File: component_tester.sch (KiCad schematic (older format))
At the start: 87 parts, among them IC1 ATMEGA16U2, IC2 ATMEGA328P-A, P1 USB_OTG, P10 ICSP_prog_16u2_4, P11 BO_PC6, P12 ICSP_prog_16u2_5, P13 BO_PC5, P14 BO_PD2, P15 BO_PD3, P16 BO_PD4, P17 BO_PD5, P18 BO_PD6, P19 ICSP_prog_328_1, P2 BATTERY_CONNECTOR, P20 ICSP_prog_328_3, P21 ICSP_prog_328_4, P22 ICSP_prog_328_5, P23 CONN_01X01, P24 Device Under Test, P25 CONN_01X03, P3 Voltage_for_zener, P4 BO_PC7, P5 ICSP_prog_16u2_1, P6 BO_PD0, P7 BO_PD1, P8 BO_PC4, P9 ICSP_prog_16u2_3, Q1 TRANSISTOR_NPN_2N2222_KSP222A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, SW1 ON-OFF switch, SW2 DO_MEASUREMENT, SW3 CONNECT_CAP, U1 NCP1117ST50T3G, U2 XF2L-2625-1A, U3 LT1004, U4 CDSOT23-SRV05-4, Y1 8MHz, Y2 16MHz

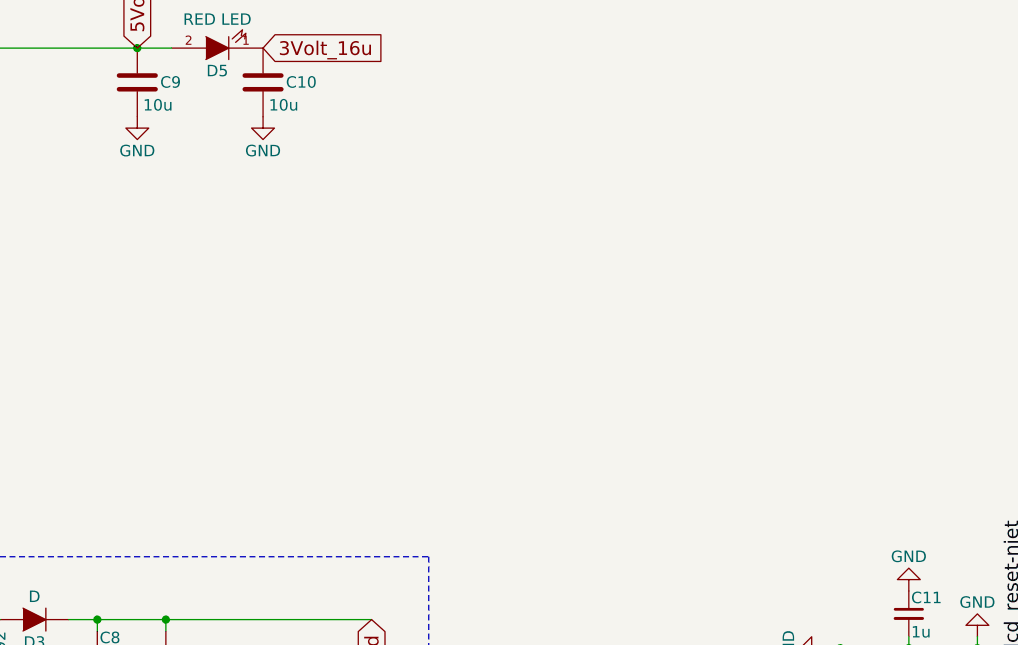
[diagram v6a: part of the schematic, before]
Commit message: Added voltage regulator option
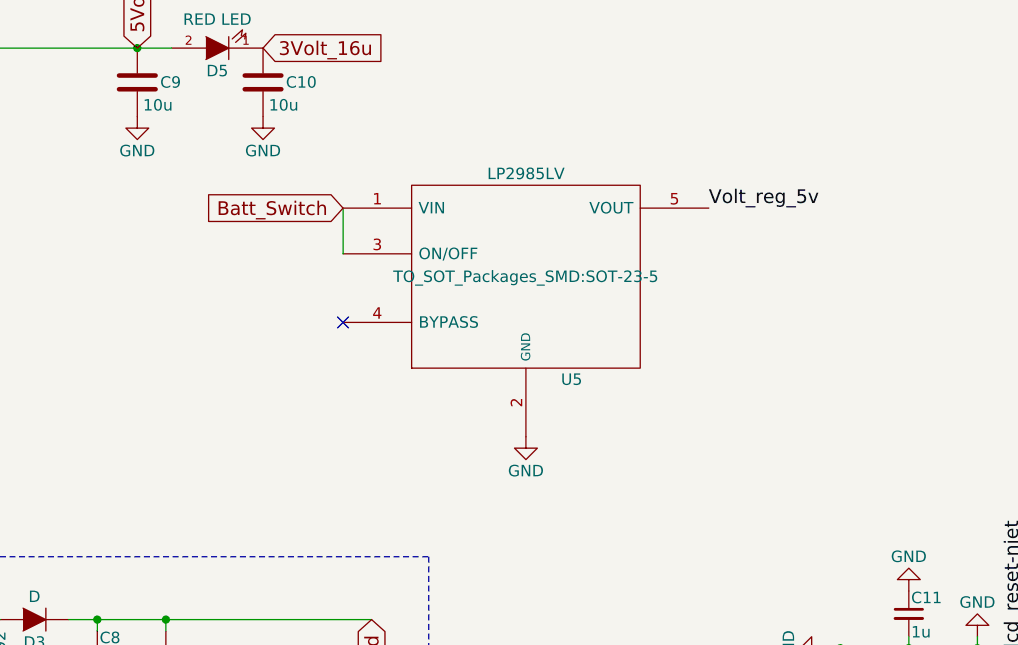
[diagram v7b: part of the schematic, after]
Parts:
- added U5: LP2985LV, TO_SOT_Packages_SMD:SOT-23-5, symbol LP2985LV
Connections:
- net Batt_Switch: now also U5.1 (VIN), U5.3 (ON/OFF)
- net GND: now also U5.2 (GND)
- net Volt_reg_5v: now also U5.5 (VOUT)
- no-connect marks 11 -> 12
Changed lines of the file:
@@
 $EndComp
 $Comp
-L GND #PWR01
+L GND #PWR27
 U 1 1 575F0F51
 P 8050 4450
-F 0 "#PWR01" H 8050 4200 50  0001 C CNN
+F 0 "#PWR27" H 8050 4200 50  0001 C CNN
 F 1 "GND" H 8050 4300 50  0000 C CNN
 F 2 "" H 8050 4450 50  0000 C CNN
@@
 $EndComp
 $Comp
-L GND #PWR02
+L GND #PWR30
 U 1 1 575F0FE6
 P 8550 6200
-F 0 "#PWR02" H 8550 5950 50  0001 C CNN
+F 0 "#PWR30" H 8550 5950 50  0001 C CNN
 F 1 "GND" H 8550 6050 50  0000 C CNN
 F 2 "" H 8550 6200 50  0000 C CNN
@@
 $EndComp
 $Comp
-L GND #PWR03
+L GND #PWR33
 U 1 1 575F1827
 P 11125 4525
-F 0 "#PWR03" H 11125 4275 50  0001 C CNN
+F 0 "#PWR33" H 11125 4275 50  0001 C CNN
 F 1 "GND" H 11125 4375 50  0000 C CNN
 F 2 "" H 11125 4525 50  0000 C CNN
@@
 3Volt_16u
 $Comp
-L GND #PWR04
+L GND #PWR18
 U 1 1 575F30CE
 P 4000 4900
-F 0 "#PWR04" H 4000 4650 50  0001 C CNN
+F 0 "#PWR18" H 4000 4650 50  0001 C CNN
 F 1 "GND" H 4000 4750 50  0000 C CNN
 F 2 "" H 4000 4900 50  0000 C CNN
@@
 $EndComp
 $Comp
-L GND #PWR05
+L GND #PWR7
 U 1 1 575F3C8E
 P 2175 3200
-F 0 "#PWR05" H 2175 2950 50  0001 C CNN
+F 0 "#PWR7" H 2175 2950 50  0001 C CNN
 F 1 "GND" H 2175 3050 50  0000 C CNN
 F 2 "" H 2175 3200 50  0000 C CNN
@@
 $EndComp
 $Comp
-L GND #PWR06
+L GND #PWR13
 U 1 1 575F41D4
 P 2900 4100
-F 0 "#PWR06" H 2900 3850 50  0001 C CNN
+F 0 "#PWR13" H 2900 3850 50  0001 C CNN
 F 1 "GND" H 2900 3950 50  0000 C CNN
 F 2 "" H 2900 4100 50  0000 C CNN
@@
 $EndComp
 $Comp
-L GND #PWR07
+L GND #PWR1
 U 1 1 575F4FF7
 P 725 3500
-F 0 "#PWR07" H 725 3250 50  0001 C CNN
+F 0 "#PWR1" H 725 3250 50  0001 C CNN
 F 1 "GND" H 725 3350 50  0000 C CNN
 F 2 "" H 725 3500 50  0000 C CNN
@@
 $EndComp
 $Comp
-L GND #PWR08
+L GND #PWR5
 U 1 1 575F552B
 P 1850 4350
-F 0 "#PWR08" H 1850 4100 50  0001 C CNN
+F 0 "#PWR5" H 1850 4100 50  0001 C CNN
 F 1 "GND" H 1850 4200 50  0000 C CNN
 F 2 "" H 1850 4350 50  0000 C CNN
@@
 $EndComp
 $Comp
-L GND #PWR09
+L GND #PWR4
 U 1 1 575F556D
 P 1625 4350
-F 0 "#PWR09" H 1625 4100 50  0001 C CNN
+F 0 "#PWR4" H 1625 4100 50  0001 C CNN
 F 1 "GND" H 1625 4200 50  0000 C CNN
 F 2 "" H 1625 4350 50  0000 C CNN
@@
 USB_Vcc
 $Comp
-L GND #PWR010
+L GND #PWR2
 U 1 1 575F563D
 P 1125 3700
-F 0 "#PWR010" H 1125 3450 50  0001 C CNN
+F 0 "#PWR2" H 1125 3450 50  0001 C CNN
 F 1 "GND" H 1125 3550 50  0000 C CNN
 F 2 "" H 1125 3700 50  0000 C CNN
@@
 $EndComp
 $Comp
-L GND #PWR011
+L GND #PWR15
 U 1 1 575F65D9
 P 3550 5750
-F 0 "#PWR011" H 3550 5500 50  0001 C CNN
+F 0 "#PWR15" H 3550 5500 50  0001 C CNN
 F 1 "GND" H 3550 5600 50  0000 C CNN
 F 2 "" H 3550 5750 50  0000 C CNN
@@
 5Volt_328
 $Comp
-L GND #PWR012
+L GND #PWR36
 U 1 1 575FC633
 P 12800 2225
-F 0 "#PWR012" H 12800 1975 50  0001 C CNN
+F 0 "#PWR36" H 12800 1975 50  0001 C CNN
 F 1 "GND" H 12800 2075 50  0000 C CNN
 F 2 "" H 12800 2225 50  0000 C CNN
@@
 $EndComp
 $Comp
-L GND #PWR013
+L GND #PWR8
 U 1 1 575FFAE7
 P 2350 3700
-F 0 "#PWR013" H 2350 3450 50  0001 C CNN
+F 0 "#PWR8" H 2350 3450 50  0001 C CNN
 F 1 "GND" H 2350 3550 50  0000 C CNN
 F 2 "" H 2350 3700 50  0000 C CNN
@@
 Battery_input
 $Comp
-L GND #PWR014
+L GND #PWR3
 U 1 1 576121F6
 P 1200 7000
-F 0 "#PWR014" H 1200 6750 50  0001 C CNN
+F 0 "#PWR3" H 1200 6750 50  0001 C CNN
 F 1 "GND" H 1200 6850 50  0000 C CNN
 F 2 "" H 1200 7000 50  0000 C CNN
@@
 $EndComp
 $Comp
-L GND #PWR015
+L GND #PWR21
 U 1 1 57613538
 P 4575 6575
-F 0 "#PWR015" H 4575 6325 50  0001 C CNN
+F 0 "#PWR21" H 4575 6325 50  0001 C CNN
 F 1 "GND" H 4575 6425 50  0000 C CNN
 F 2 "" H 4575 6575 50  0000 C CNN
@@
 $EndComp
 $Comp
-L GND #PWR016
+L GND #PWR22
 U 1 1 5761377B
 P 5125 6575
-F 0 "#PWR016" H 5125 6325 50  0001 C CNN
+F 0 "#PWR22" H 5125 6325 50  0001 C CNN
 F 1 "GND" H 5125 6425 50  0000 C CNN
 F 2 "" H 5125 6575 50  0000 C CNN
@@
 $EndComp
 $Comp
-L GND #PWR017
+L GND #PWR25
 U 1 1 5761F9F4
 P 7850 3125
-F 0 "#PWR017" H 7850 2875 50  0001 C CNN
+F 0 "#PWR25" H 7850 2875 50  0001 C CNN
 F 1 "GND" H 7850 2975 50  0000 C CNN
 F 2 "" H 7850 3125 50  0000 C CNN
@@
 $EndComp
 $Comp
-L GND #PWR018
+L GND #PWR35
 U 1 1 57622493
 P 11850 5925
-F 0 "#PWR018" H 11850 5675 50  0001 C CNN
+F 0 "#PWR35" H 11850 5675 50  0001 C CNN
 F 1 "GND" H 11850 5775 50  0000 C CNN
 F 2 "" H 11850 5925 50  0000 C CNN
@@
 $EndComp
 $Comp
-L GND #PWR019
+L GND #PWR16
 U 1 1 576263B2
 P 3650 2000
-F 0 "#PWR019" H 3650 1750 50  0001 C CNN
+F 0 "#PWR16" H 3650 1750 50  0001 C CNN
 F 1 "GND" H 3650 1850 50  0000 C CNN
 F 2 "" H 3650 2000 50  0000 C CNN
@@
 3Volt_16u
 $Comp
-L GND #PWR020
+L GND #PWR31
 U 1 1 57602456
 P 9550 8900
-F 0 "#PWR020" H 9550 8650 50  0001 C CNN
+F 0 "#PWR31" H 9550 8650 50  0001 C CNN
 F 1 "GND" H 9550 8750 50  0000 C CNN
 F 2 "" H 9550 8900 50  0000 C CNN
@@
 lcd_reset-niet
 $Comp
-L GND #PWR021
+L GND #PWR29
 U 1 1 5760820F
 P 8250 8850
-F 0 "#PWR021" H 8250 8600 50  0001 C CNN
+F 0 "#PWR29" H 8250 8600 50  0001 C CNN
 F 1 "GND" H 8250 8700 50  0000 C CNN
 F 2 "" H 8250 8850 50  0000 C CNN
@@
 $EndComp
 $Comp
-L GND #PWR022
+L GND #PWR26
 U 1 1 57608825
 P 7950 8650
-F 0 "#PWR022" H 7950 8400 50  0001 C CNN
+F 0 "#PWR26" H 7950 8400 50  0001 C CNN
 F 1 "GND" H 7950 8500 50  0000 C CNN
 F 2 "" H 7950 8650 50  0000 C CNN
@@
 $EndComp
 $Comp
-L GND #PWR023
+L GND #PWR24
 U 1 1 57608AFA
 P 7575 8900
-F 0 "#PWR023" H 7575 8650 50  0001 C CNN
+F 0 "#PWR24" H 7575 8650 50  0001 C CNN
 F 1 "GND" H 7575 8750 50  0000 C CNN
 F 2 "" H 7575 8900 50  0000 C CNN
@@
 $EndComp
 $Comp
-L GND #PWR024
+L GND #PWR9
 U 1 1 57611855
 P 2500 5100
-F 0 "#PWR024" H 2500 4850 50  0001 C CNN
+F 0 "#PWR9" H 2500 4850 50  0001 C CNN
 F 1 "GND" H 2500 4950 50  0000 C CNN
 F 2 "" H 2500 5100 50  0000 C CNN
@@
 $EndComp
 $Comp
-L GND #PWR025
+L GND #PWR10
 U 1 1 576118BF
 P 2500 6150
-F 0 "#PWR025" H 2500 5900 50  0001 C CNN
+F 0 "#PWR10" H 2500 5900 50  0001 C CNN
 F 1 "GND" H 2500 6000 50  0000 C CNN
 F 2 "" H 2500 6150 50  0000 C CNN
@@
 $EndComp
 $Comp
-L GND #PWR026
+L GND #PWR14
 U 1 1 57613EBC
 P 3125 5700
-F 0 "#PWR026" H 3125 5450 50  0001 C CNN
+F 0 "#PWR14" H 3125 5450 50  0001 C CNN
 F 1 "GND" H 3125 5575 50  0000 C CNN
 F 2 "" H 3125 5700 50  0000 C CNN
@@
 $EndComp
 $Comp
-L GND #PWR027
+L GND #PWR19
 U 1 1 57613F2A
 P 4050 5700
-F 0 "#PWR027" H 4050 5450 50  0001 C CNN
+F 0 "#PWR19" H 4050 5450 50  0001 C CNN
 F 1 "GND" H 4050 5550 50  0000 C CNN
 F 2 "" H 4050 5700 50  0000 C CNN
@@
 $EndComp
 $Comp
-L GND #PWR028
+L GND #PWR34
 U 1 1 5761A67A
 P 11125 6600
-F 0 "#PWR028" H 11125 6350 50  0001 C CNN
+F 0 "#PWR34" H 11125 6350 50  0001 C CNN
 F 1 "GND" H 11125 6450 50  0000 C CNN
 F 2 "" H 11125 6600 50  0000 C CNN
@@
 $EndComp
 $Comp
-L GND #PWR029
+L GND #PWR11
 U 1 1 5761C1A3
 P 2800 7950
-F 0 "#PWR029" H 2800 7700 50  0001 C CNN
+F 0 "#PWR11" H 2800 7700 50  0001 C CNN
 F 1 "GND" H 2800 7800 50  0000 C CNN
 F 2 "" H 2800 7950 50  0000 C CNN
@@
 $EndComp
 $Comp
-L GND #PWR030
+L GND #PWR28
 U 1 1 576269FA
 P 8225 3850
-F 0 "#PWR030" H 8225 3600 50  0001 C CNN
+F 0 "#PWR28" H 8225 3600 50  0001 C CNN
 F 1 "GND" H 8225 3700 50  0000 C CNN
 F 2 "" H 8225 3850 50  0000 C CNN
@@
 NoConn ~ 14750 8875
 $Comp
-L GND #PWR031
+L GND #PWR37
 U 1 1 5763156B
 P 14050 9025
-F 0 "#PWR031" H 14050 8775 50  0001 C CNN
+F 0 "#PWR37" H 14050 8775 50  0001 C CNN
 F 1 "GND" H 14050 8875 50  0000 C CNN
 F 2 "" H 14050 9025 50  0000 C CNN
@@
 	2875 9050 2875 9125
 $Comp
-L GND #PWR032
+L GND #PWR12
 U 1 1 576365B7
 P 2875 9125
-F 0 "#PWR032" H 2875 8875 50  0001 C CNN
+F 0 "#PWR12" H 2875 8875 50  0001 C CNN
 F 1 "GND" H 2875 8975 50  0000 C CNN
 F 2 "" H 2875 9125 50  0000 C CNN
@@
 Connection ~ 2875 8775
 $Comp
-L GND #PWR033
+L GND #PWR17
 U 1 1 5763757B
 P 3850 9225
-F 0 "#PWR033" H 3850 8975 50  0001 C CNN
+F 0 "#PWR17" H 3850 8975 50  0001 C CNN
 F 1 "GND" H 3850 9075 50  0000 C CNN
 F 2 "" H 3850 9225 50  0000 C CNN
@@
 	4400 9225 4700 9225
 $Comp
-L GND #PWR034
+L GND #PWR20
 U 1 1 5763BF7F
 P 4550 9275
-F 0 "#PWR034" H 4550 9025 50  0001 C CNN
+F 0 "#PWR20" H 4550 9025 50  0001 C CNN
 F 1 "GND" H 4550 9125 50  0000 C CNN
 F 2 "" H 4550 9275 50  0000 C CNN
@@
 $EndComp
 $Comp
-L GND #PWR035
+L GND #PWR32
 U 1 1 576B1814
 P 9950 8375
-F 0 "#PWR035" H 9950 8125 50  0001 C CNN
+F 0 "#PWR32" H 9950 8125 50  0001 C CNN
 F 1 "GND" H 9950 8225 50  0000 C CNN
 F 2 "" H 9950 8375 50  0000 C CNN
@@
 $EndComp
 $Comp
-L GND #PWR036
+L GND #PWR6
 U 1 1 576E83D7
 P 1900 3200
-F 0 "#PWR036" H 1900 2950 50  0001 C CNN
+F 0 "#PWR6" H 1900 2950 50  0001 C CNN
 F 1 "GND" H 1900 3050 50  0000 C CNN
 F 2 "" H 1900 3200 50  0000 C CNN
@@
 	1900 3600 1900 3800
 Connection ~ 1900 3800
+$Comp
+L LP2985LV U5
+U 1 1 576F0470
+P 6275 7275
+F 0 "U5" H 6475 6825 50  0000 C CNN
+F 1 "LP2985LV" H 6275 7725 50  0000 C CNN
+F 2 "TO_SOT_Packages_SMD:SOT-23-5" H 6275 7275 50  0000 C CNN
+F 3 "" H 6275 7275 50  0000 C CNN
+	1    6275 7275
+	1    0    0    -1
+$EndComp
+Text GLabel 5475 6975 0    60   Input ~ 0
+Batt_Switch
+Text Label 7075 6975 0    60   ~ 0
+Volt_reg_5v
+$Comp
+L GND #PWR23
+U 1 1 576F0B2D
+P 6275 7975
+F 0 "#PWR23" H 6275 7725 50  0001 C CNN
+F 1 "GND" H 6275 7825 50  0000 C CNN
+F 2 "" H 6275 7975 50  0000 C CNN
+F 3 "" H 6275 7975 50  0000 C CNN
+	1    6275 7975
+	1    0    0    -1
+$EndComp
+Wire Wire Line
+	5475 7175 5475 6975
+NoConn ~ 5475 7475
 $EndSCHEMATC

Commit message: Added the possibility of using a different LDO voltage regulator.
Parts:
- U1: symbol NCP1117ST50T3G -> LT1129IST-5
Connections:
- net Batt_Switch: now also U1.1 (VIN); no longer U1.3 (VI)
- net GND: now also U1.2 (GND); no longer U1.1 (GND)
- net Volt_reg_5v: now also U1.3 (OUT); no longer U1.2 (VO)
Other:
- moved on the sheet: C7, U1
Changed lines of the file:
@@
 L GND #PWR15
 U 1 1 575F65D9
-P 3550 5750
-F 0 "#PWR15" H 3550 5500 50  0001 C CNN
-F 1 "GND" H 3550 5600 50  0000 C CNN
-F 2 "" H 3550 5750 50  0000 C CNN
-F 3 "" H 3550 5750 50  0000 C CNN
-	1    3550 5750
+P 3600 5800
+F 0 "#PWR15" H 3600 5550 50  0001 C CNN
+F 1 "GND" H 3600 5650 50  0000 C CNN
+F 2 "" H 3600 5800 50  0000 C CNN
+F 3 "" H 3600 5800 50  0000 C CNN
+	1    3600 5800
 	1    0    0    -1
 $EndComp
@@
 $EndComp
 $Comp
-L NCP1117ST50T3G U1
+L LT1129IST-5 U1
 U 1 1 57613AAF
-P 3550 5500
-F 0 "U1" H 3550 5775 50  0000 C CNN
-F 1 "NCP1117ST50T3G" H 3550 5700 50  0000 C CNN
-F 2 "TO_SOT_Packages_SMD:SOT-223" H 3550 5500 50  0001 C CNN
-F 3 "" H 3550 5500 50  0000 C CNN
-	1    3550 5500
+P 3600 5500
+F 0 "U1" H 3600 5775 50  0000 C CNN
+F 1 "NCP1117ST50T3G" H 3600 5700 50  0000 C CNN
+F 2 "TO_SOT_Packages_SMD:SOT-223" H 3600 5500 50  0001 C CNN
+F 3 "" H 3600 5500 50  0000 C CNN
+	1    3600 5500
 	1    0    0    -1
 $EndComp
@@
 L C_Small C7
 U 1 1 57613DF7
-P 4050 5575
-F 0 "C7" H 4060 5645 50  0000 L CNN
-F 1 "10u" H 4060 5495 50  0000 L CNN
-F 2 "Capacitors_SMD:C_0805_HandSoldering" H 4050 5575 50  0001 C CNN
-F 3 "" H 4050 5575 50  0000 C CNN
-	1    4050 5575
+P 4125 5575
+F 0 "C7" H 4135 5645 50  0000 L CNN
+F 1 "10u" H 4135 5495 50  0000 L CNN
+F 2 "Capacitors_SMD:C_0805_HandSoldering" H 4125 5575 50  0001 C CNN
+F 3 "" H 4125 5575 50  0000 C CNN
+	1    4125 5575
 	1    0    0    -1
 $EndComp
@@
 L GND #PWR19
 U 1 1 57613F2A
-P 4050 5700
-F 0 "#PWR19" H 4050 5450 50  0001 C CNN
-F 1 "GND" H 4050 5550 50  0000 C CNN
-F 2 "" H 4050 5700 50  0000 C CNN
-F 3 "" H 4050 5700 50  0000 C CNN
-	1    4050 5700
+P 4125 5700
+F 0 "#PWR19" H 4125 5450 50  0001 C CNN
+F 1 "GND" H 4125 5550 50  0000 C CNN
+F 2 "" H 4125 5700 50  0000 C CNN
+F 3 "" H 4125 5700 50  0000 C CNN
+	1    4125 5700
 	1    0    0    -1
 $EndComp
@@
 	11800 5675 11850 5675
 Connection ~ 11850 5675
-Wire Wire Line
-	3950 5450 4225 5450
-Wire Wire Line
-	4050 5475 4050 5450
-Connection ~ 4050 5450
-Wire Wire Line
-	4050 5675 4050 5700
 Connection ~ 4575 6275
 Wire Wire Line
@@
 	5475 7175 5475 6975
 NoConn ~ 5475 7475
+Wire Wire Line
+	4225 5450 4050 5450
+Wire Wire Line
+	4125 5475 4125 5450
+Connection ~ 4125 5450
+Wire Wire Line
+	4125 5700 4125 5675
 $EndSCHEMATC
